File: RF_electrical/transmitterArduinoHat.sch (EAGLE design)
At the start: 55 parts

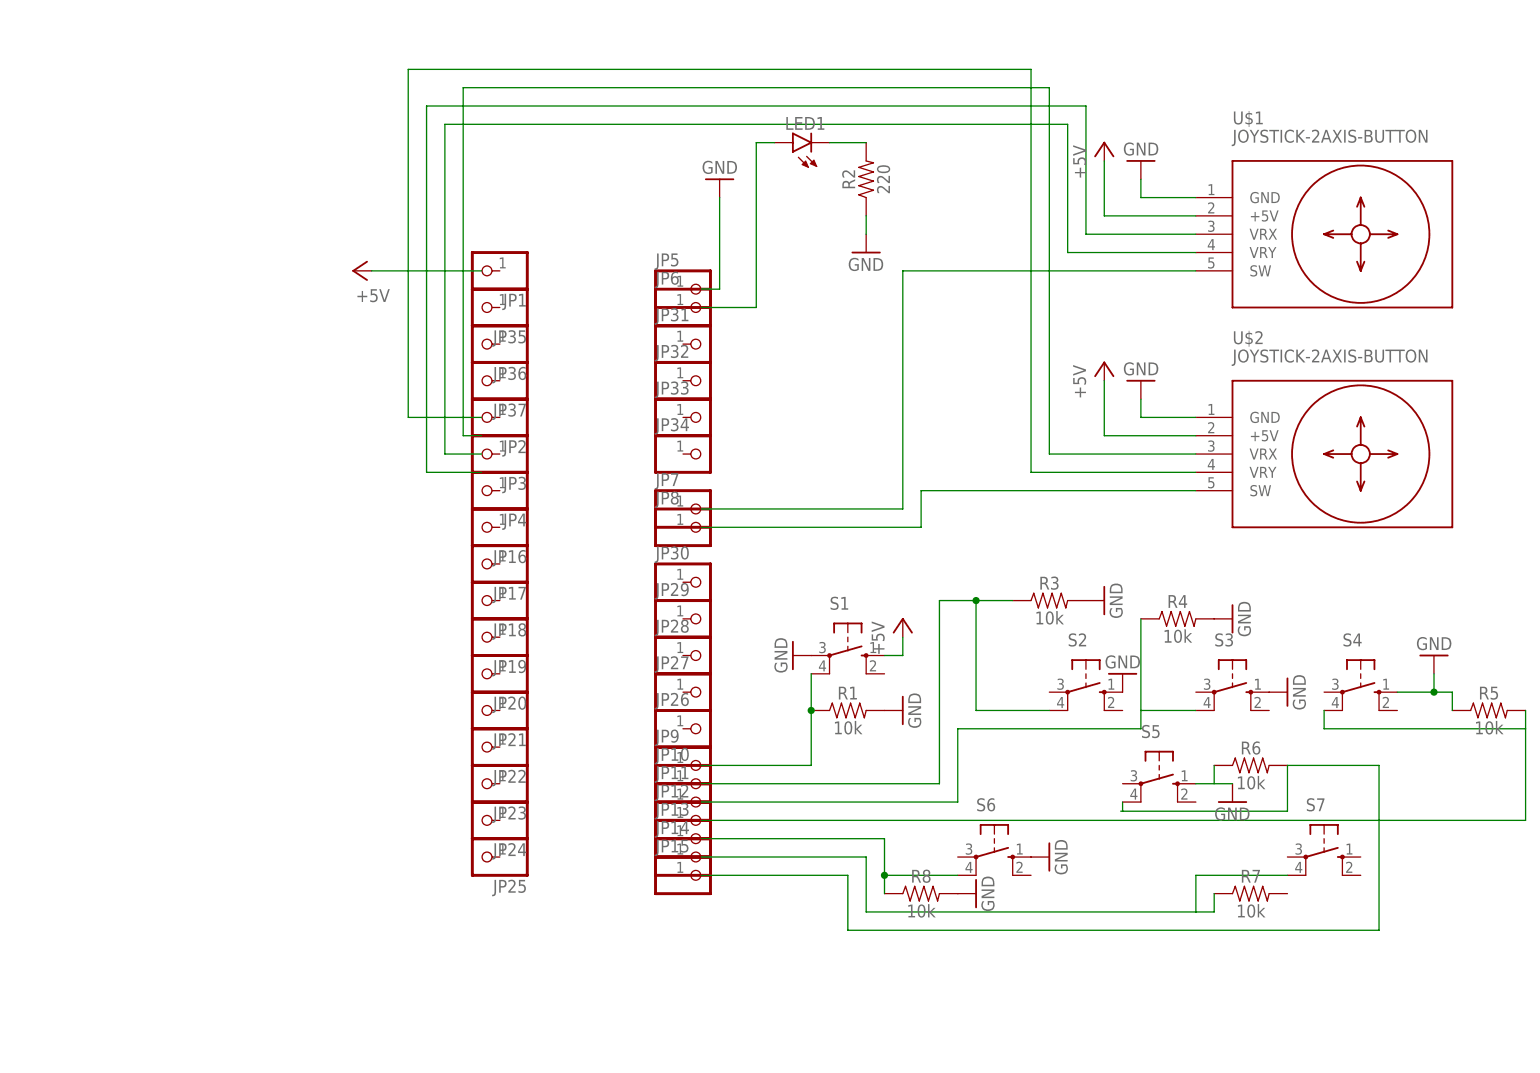
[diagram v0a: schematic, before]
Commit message: Changed status light to RGB and modified resistors
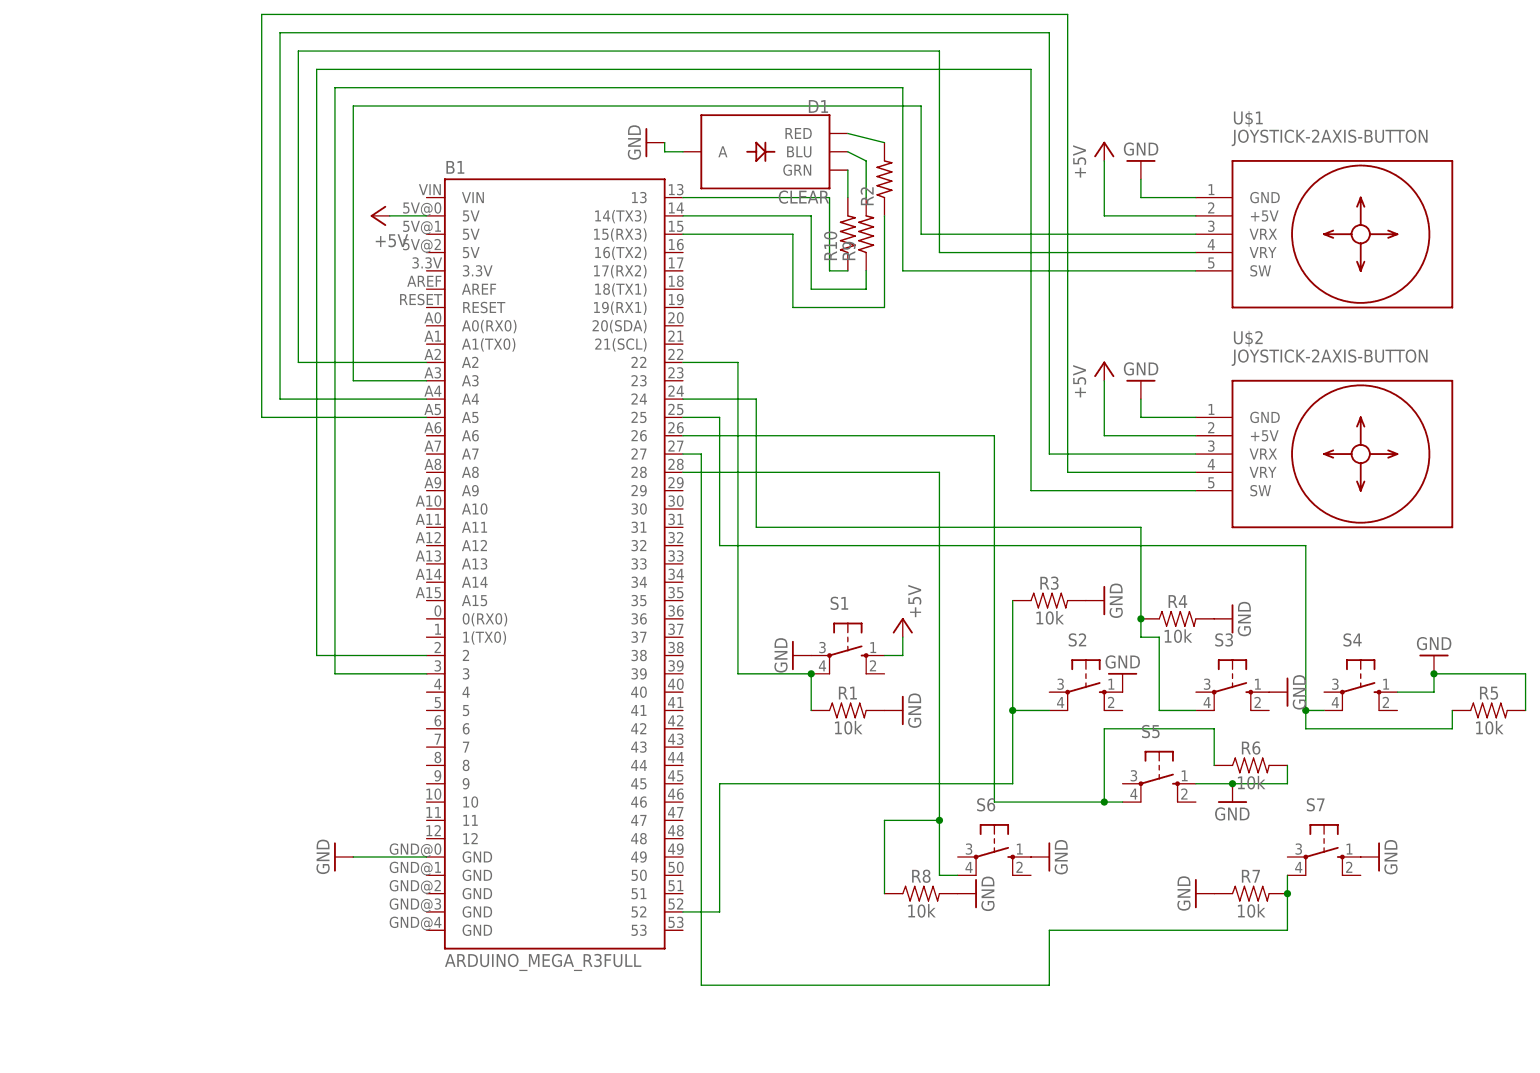
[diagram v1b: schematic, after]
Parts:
- removed JP1, JP10, JP11, JP12, JP13, JP14, JP15, JP16, JP17, JP18, JP19, JP2, JP20, JP21, JP22, JP23, JP24, JP25, JP26, JP27, JP28, JP29, JP3, JP30, JP31, JP32, JP33, JP34, JP35, JP36, JP37, JP4, JP5, JP6, JP7, JP8, JP9: (no value), pinhead:PINHD-1X1
- removed LED1: (no value), led:LED3MM
- added B1: ARDUINO_MEGA_R3FULL, SparkFun-Boards:ARDUINO_MEGA_R3FULL
- added D1: CLEAR, SparkFun-LED:LED-RGB-CACLEAR
- added R10, R9: (no value), rcl:R-US_V234/12
- R2: value 220 -> (none); device SparkFun-Resistors:220OHM-0603-1/10W-1% -> rcl:R-US_V234/12
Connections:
- removed net N$14: R7.1, S7.P1
- new net N$17: B1.A3, U$1.VRX
- new net N$18: B1.A2, U$1.VRY
- new net N$19: B1.A4, U$2.VRX
- new net N$20: B1.A5, U$2.VRY
- net +5V: now also B1.5V@0
- net GND: now also B1.GND@0, D1.A, R5.2, R6.2, R7.1, S7.S; no longer R2.1, R5.1
- net N$1: now also D1.BLU, R9.2; no longer LED1.A
- net N$10: now also B1.26, R6.1, S5.P1; no longer R1.1, S1.P1
- net N$11: now also B1.15(RX3), R2.1; no longer R4.1, S3.P1
- net N$12: now also B1.27, R7.2, S7.P1; no longer R5.2, S4.P1
- net N$13: now also B1.28
- net N$15: now also B1.3, U$1.SW; no longer R6.2, S5.P1
- net N$16: now also B1.2, U$2.SW; no longer R6.1
- net N$2: now also D1.RED; no longer LED1.C
- net N$3: now also B1.22, R1.1, S1.P1; no longer U$1.VRX
- net N$4: now also B1.52, R3.1, S2.P1; no longer U$1.VRY
- net N$5: now also D1.GRN, R10.2; no longer U$1.SW
- net N$6: now also B1.24, R4.1, S3.P1; no longer U$2.SW
- net N$7: now also B1.25, R5.1, S4.P1; no longer U$2.VRX
- net N$8: now also B1.13, R10.1; no longer U$2.VRY
- net N$9: now also B1.14(TX3), R9.1; no longer R3.1, S2.P1
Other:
- moved on the sheet: R2

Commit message: Added RF device to schematic & PCB. Starting to create prototype cpp program on Arduino.
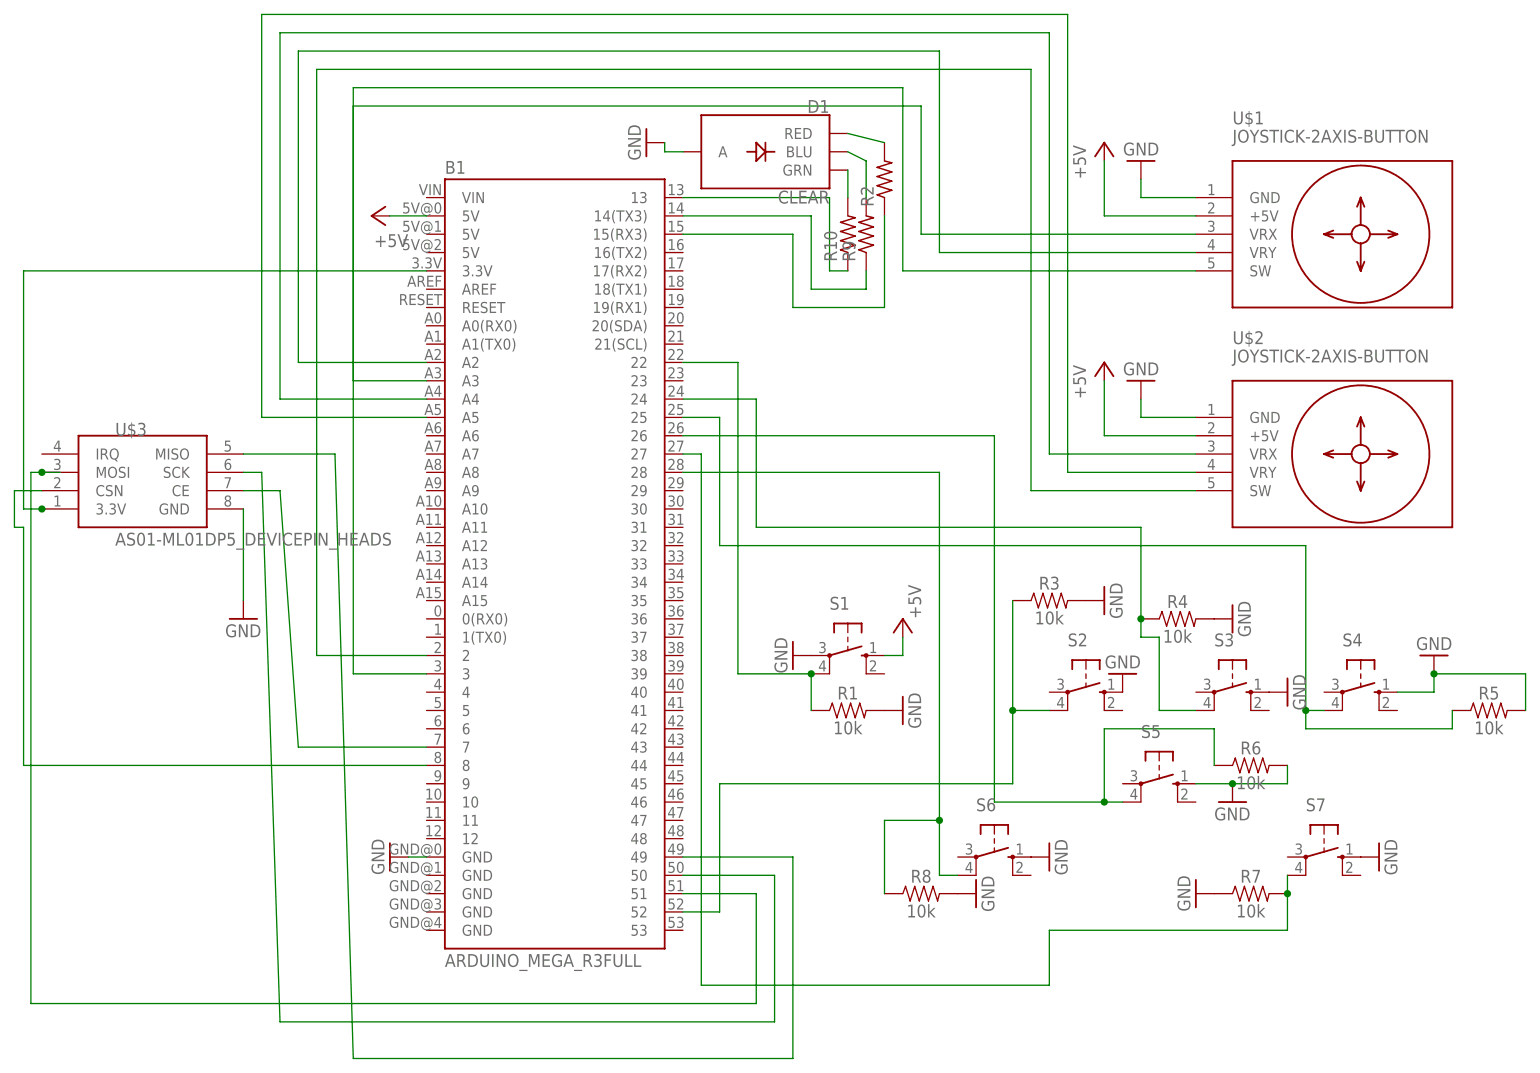
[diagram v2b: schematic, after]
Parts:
- added U$3: AS01-ML01DP5_DEVICEPIN_HEADS, diy01-arduino-library:AS01-ML01DP5_DEVICEPIN_HEADS
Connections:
- new net N$14: B1.3.3V, U$3.3.3V
- new net N$21: B1.8, U$3.CSN
- new net N$22: B1.7, U$3.CE
- new net N$23: B1.51, U$3.MOSI
- new net N$24: B1.50, U$3.SCK
- new net N$25: B1.49, U$3.MISO
- net GND: now also U$3.GND
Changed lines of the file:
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@@
 <part name="R9" library="rcl" library_urn="urn:adsk.eagle:library:334" deviceset="R-US_" device="V234/12" package3d_urn="urn:adsk.eagle:package:23592/1"/>
 <part name="R10" library="rcl" library_urn="urn:adsk.eagle:library:334" deviceset="R-US_" device="V234/12" package3d_urn="urn:adsk.eagle:package:23592/1"/>
+<part name="GND17" library="supply1" library_urn="urn:adsk.eagle:library:371" deviceset="GND" device=""/>
+<part name="U$3" library="diy01-arduino-library" deviceset="AS01-ML01DP5_DEVICE" device="PIN_HEADS" package3d_urn="urn:adsk.eagle:package:21263681/1"/>
 </parts>
 <sheets>
@@
 <attribute name="VALUE" x="127" y="41.656" size="1.778" layer="96" font="vector" align="top-center"/>
 </instance>
-<instance part="GND1" gate="1" x="45.72" y="48.26" smashed="yes" rot="R270">
-<attribute name="VALUE" x="43.18" y="50.8" size="1.778" layer="96" rot="R270"/>
+<instance part="GND1" gate="1" x="53.34" y="48.26" smashed="yes" rot="R270">
+<attribute name="VALUE" x="50.8" y="50.8" size="1.778" layer="96" rot="R270"/>
 </instance>
 <instance part="GND2" gate="1" x="88.9" y="147.32" smashed="yes" rot="R270">
@@
 <attribute name="NAME" x="115.3414" y="130.81" size="1.778" layer="95" rot="R90"/>
 <attribute name="VALUE" x="120.142" y="130.81" size="1.778" layer="96" rot="R90"/>
+</instance>
+<instance part="GND17" gate="1" x="33.02" y="81.28" smashed="yes">
+<attribute name="VALUE" x="30.48" y="78.74" size="1.778" layer="96"/>
+</instance>
+<instance part="U$3" gate="G$1" x="53.34" y="83.82" smashed="yes">
+<attribute name="VALUE" x="15.24" y="91.44" size="1.778" layer="96"/>
+<attribute name="NAME" x="15.24" y="106.68" size="1.778" layer="95"/>
 </instance>
 </instances>
@@
 <pinref part="B1" gate="G$1" pin="GND@0"/>
 <pinref part="GND1" gate="1" pin="GND"/>
-<wire x1="58.42" y1="48.26" x2="48.26" y2="48.26" width="0.1524" layer="91"/>
+<wire x1="58.42" y1="48.26" x2="55.88" y2="48.26" width="0.1524" layer="91"/>
 </segment>
 <segment>
@@
 <wire x1="93.98" y1="146.05" x2="91.44" y2="146.05" width="0.1524" layer="91"/>
 <wire x1="91.44" y1="146.05" x2="91.44" y2="147.32" width="0.1524" layer="91"/>
+</segment>
+<segment>
+<pinref part="GND17" gate="1" pin="GND"/>
+<wire x1="33.02" y1="83.82" x2="33.02" y2="96.52" width="0.1524" layer="91"/>
+<pinref part="U$3" gate="G$1" pin="GND"/>
 </segment>
 </net>
@@
 <wire x1="165.1" y1="129.54" x2="124.46" y2="129.54" width="0.1524" layer="91"/>
 <wire x1="124.46" y1="129.54" x2="124.46" y2="154.94" width="0.1524" layer="91"/>
-<wire x1="124.46" y1="154.94" x2="45.72" y2="154.94" width="0.1524" layer="91"/>
-<wire x1="45.72" y1="154.94" x2="45.72" y2="73.66" width="0.1524" layer="91"/>
+<wire x1="124.46" y1="154.94" x2="48.26" y2="154.94" width="0.1524" layer="91"/>
+<wire x1="48.26" y1="154.94" x2="48.26" y2="73.66" width="0.1524" layer="91"/>
 <pinref part="B1" gate="G$1" pin="3"/>
-<wire x1="45.72" y1="73.66" x2="58.42" y2="73.66" width="0.1524" layer="91"/>
+<wire x1="48.26" y1="73.66" x2="58.42" y2="73.66" width="0.1524" layer="91"/>
 </segment>
 </net>
@@
 </segment>
 </net>
+<net name="N$14" class="0">
+<segment>
+<wire x1="5.08" y1="96.52" x2="2.54" y2="96.52" width="0.1524" layer="91"/>
+<wire x1="2.54" y1="96.52" x2="2.54" y2="129.54" width="0.1524" layer="91"/>
+<pinref part="B1" gate="G$1" pin="3.3V"/>
+<wire x1="2.54" y1="129.54" x2="58.42" y2="129.54" width="0.1524" layer="91"/>
+<pinref part="U$3" gate="G$1" pin="3.3V"/>
+<junction x="5.08" y="96.52"/>
+</segment>
+</net>
+<net name="N$21" class="0">
+<segment>
+<pinref part="B1" gate="G$1" pin="8"/>
+<wire x1="2.54" y1="60.96" x2="58.42" y2="60.96" width="0.1524" layer="91"/>
+<wire x1="2.54" y1="60.96" x2="2.54" y2="93.98" width="0.1524" layer="91"/>
+<wire x1="2.54" y1="93.98" x2="1.27" y2="93.98" width="0.1524" layer="91"/>
+<pinref part="U$3" gate="G$1" pin="CSN"/>
+<wire x1="1.27" y1="93.98" x2="1.27" y2="99.06" width="0.1524" layer="91"/>
+<wire x1="1.27" y1="99.06" x2="5.08" y2="99.06" width="0.1524" layer="91"/>
+</segment>
+</net>
+<net name="N$22" class="0">
+<segment>
+<wire x1="33.02" y1="99.06" x2="38.1" y2="99.06" width="0.1524" layer="91"/>
+<wire x1="38.1" y1="99.06" x2="40.64" y2="63.5" width="0.1524" layer="91"/>
+<pinref part="B1" gate="G$1" pin="7"/>
+<wire x1="40.64" y1="63.5" x2="58.42" y2="63.5" width="0.1524" layer="91"/>
+<pinref part="U$3" gate="G$1" pin="CE"/>
+</segment>
+</net>
+<net name="N$23" class="0">
+<segment>
+<wire x1="7.62" y1="101.6" x2="5.08" y2="101.6" width="0.1524" layer="91"/>
+<wire x1="5.08" y1="101.6" x2="3.556" y2="101.6" width="0.1524" layer="91"/>
+<wire x1="3.556" y1="101.6" x2="3.556" y2="27.94" width="0.1524" layer="91"/>
+<wire x1="3.556" y1="27.94" x2="104.14" y2="27.94" width="0.1524" layer="91"/>
+<pinref part="B1" gate="G$1" pin="51"/>
+<wire x1="104.14" y1="27.94" x2="104.14" y2="43.18" width="0.1524" layer="91"/>
+<wire x1="104.14" y1="43.18" x2="93.98" y2="43.18" width="0.1524" layer="91"/>
+<pinref part="U$3" gate="G$1" pin="MOSI"/>
+<junction x="5.08" y="101.6"/>
+</segment>
+</net>
+<net name="N$24" class="0">
+<segment>
+<pinref part="B1" gate="G$1" pin="50"/>
+<wire x1="93.98" y1="45.72" x2="106.68" y2="45.72" width="0.1524" layer="91"/>
+<wire x1="106.68" y1="45.72" x2="106.68" y2="25.4" width="0.1524" layer="91"/>
+<wire x1="106.68" y1="25.4" x2="38.1" y2="25.4" width="0.1524" layer="91"/>
+<wire x1="38.1" y1="25.4" x2="35.56" y2="101.6" width="0.1524" layer="91"/>
+<wire x1="35.56" y1="101.6" x2="33.02" y2="101.6" width="0.1524" layer="91"/>
+<pinref part="U$3" gate="G$1" pin="SCK"/>
+</segment>
+</net>
+<net name="N$25" class="0">
+<segment>
+<wire x1="33.02" y1="104.14" x2="45.72" y2="104.14" width="0.1524" layer="91"/>
+<wire x1="45.72" y1="104.14" x2="48.26" y2="20.32" width="0.1524" layer="91"/>
+<wire x1="48.26" y1="20.32" x2="109.22" y2="20.32" width="0.1524" layer="91"/>
+<wire x1="109.22" y1="20.32" x2="109.22" y2="48.26" width="0.1524" layer="91"/>
+<pinref part="B1" gate="G$1" pin="49"/>
+<wire x1="109.22" y1="48.26" x2="93.98" y2="48.26" width="0.1524" layer="91"/>
+<pinref part="U$3" gate="G$1" pin="MISO"/>
+</segment>
+</net>
